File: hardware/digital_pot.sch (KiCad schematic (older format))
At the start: 98 parts

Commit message: dodano wyjscie programatora, przyciski ustalono wysjcie i2c, dodany plik CubeMX z pinouterm
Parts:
- added C? (x6): 100n, symbol Device:C
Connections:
- net +5V: now also C?.2, C?.2, C?.2, C?.2, C?.2, C?.2
- net GND: now also C?.1, C?.1, C?.1, C?.1, C?.1, C?.1
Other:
- moved on the sheet: C?, R?, U?A, U?B, U?D

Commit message: DRC przechodzi dorzucone złącze do wyświetlacza na i2c oraz jeden push button
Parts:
- gave numbers to parts that had none: 80

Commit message: przypisano footprinty
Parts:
- C12, C13, C14, C15, C16, C17, C18, C19, C20, C21, C22, C23, C24, C25, C26, C27, C28, C29, C30, C31, C32, C33, C34, C35, C36, C37, C38, C39, C40, C41, C42, C43, C44, C45, C46, C47, C48, C49, C50, C51, C52, C53, C54, C55, C56, C57, C58, C59: footprint (none) -> Capacitor_SMD:C_0603_1608Metric_Pad1.05x0.95mm_HandSolder
- R10, R11, R12, R13, R14, R15, R16, R17, R18, R19, R20, R21, R6, R7, R8, R9: footprint (none) -> Resistor_SMD:R_0603_1608Metric_Pad1.05x0.95mm_HandSolder
- U10, U13, U14, U15, U16, U17, U4, U7: footprint (none) -> Package_SO:SOIC-14_3.9x8.7mm_P1.27mm

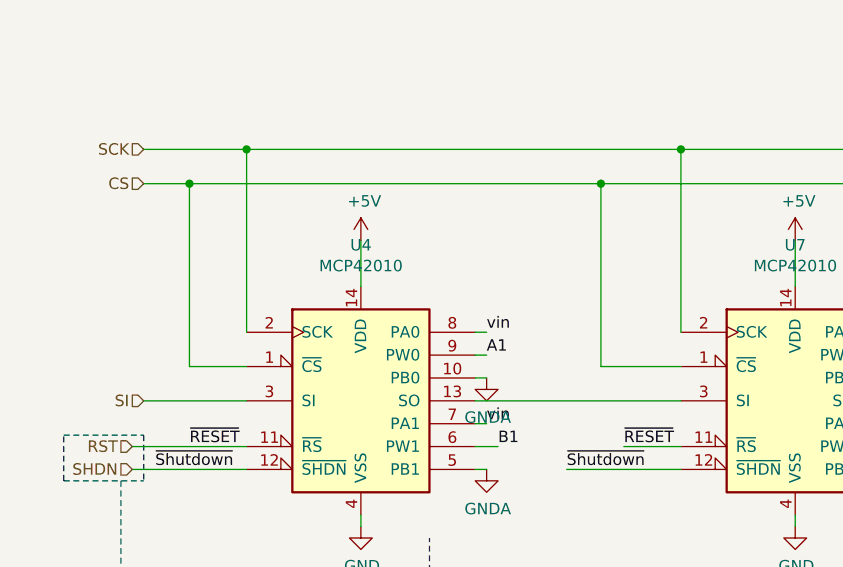
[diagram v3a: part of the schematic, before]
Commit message: Dodenie pullup do spi i i2c
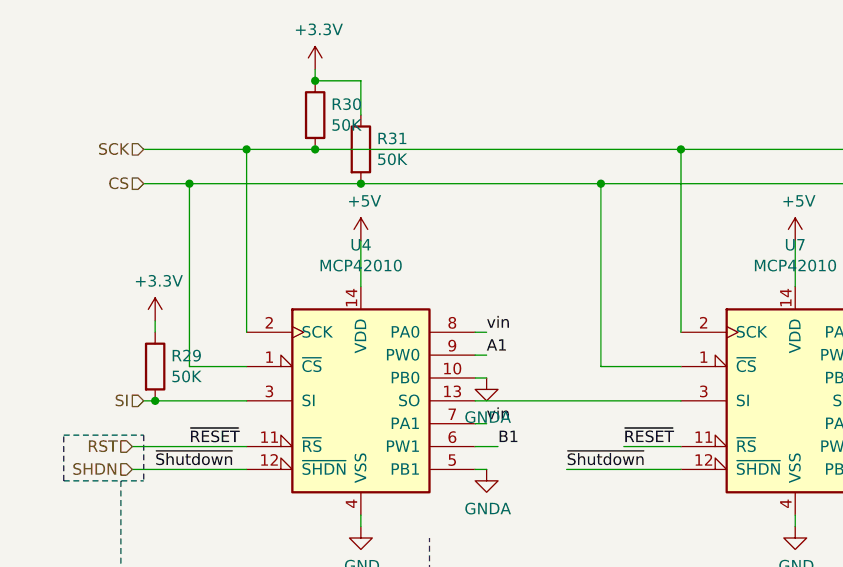
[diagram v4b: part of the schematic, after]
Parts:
- added R29, R30, R31: 50K, Resistor_SMD:R_0603_1608Metric_Pad1.05x0.95mm_HandSolder, symbol Device:R
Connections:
- net CS: now also R31.2
- net SCK: now also R30.2
- net SI: now also R29.2
- new net +3V3: R29.1, R30.1, R31.1
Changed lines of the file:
@@
 	1550 1750 1550 950
 Wire Wire Line
-	1550 950  1100 950
-Wire Wire Line
-	1550 950  3450 950
+	1550 950  1850 950
 Wire Wire Line
 	9300 950  9300 1750
@@
 	1300 1900 1550 1900
 Wire Wire Line
-	1300 1100 3100 1100
+	1300 1100 2050 1100
 Connection ~ 1300 1100
 Wire Wire Line
@@
 Connection ~ 3100 1100
 Wire Wire Line
-	1100 2050 1550 2050
+	1100 2050 1150 2050
 Text HLabel 1100 2050 0    50   Input ~ 0
 SI
@@
 Wire Wire Line
 	4700 7050 4400 7050
+$Comp
+L power:+3.3V #PWR0144
+U 1 1 5D367B76
+P 1850 600
+F 0 "#PWR0144" H 1850 450 50  0001 C CNN
+F 1 "+3.3V" H 1865 773 50  0000 C CNN
+F 2 "" H 1850 600 50  0001 C CNN
+F 3 "" H 1850 600 50  0001 C CNN
+	1    1850 600
+	1    0    0    -1
+$EndComp
+$Comp
+L Device:R R30
+U 1 1 5D36BDF5
+P 1850 800
+F 0 "R30" H 1920 846 50  0000 L CNN
+F 1 "50K" H 1920 755 50  0000 L CNN
+F 2 "Resistor_SMD:R_0603_1608Metric_Pad1.05x0.95mm_HandSolder" V 1780 800 50  0001 C CNN
+F 3 "~" H 1850 800 50  0001 C CNN
+	1    1850 800
+	1    0    0    -1
+$EndComp
+$Comp
+L Device:R R31
+U 1 1 5D36D3BE
+P 2050 950
+F 0 "R31" H 2120 996 50  0000 L CNN
+F 1 "50K" H 2120 905 50  0000 L CNN
+F 2 "Resistor_SMD:R_0603_1608Metric_Pad1.05x0.95mm_HandSolder" V 1980 950 50  0001 C CNN
+F 3 "~" H 2050 950 50  0001 C CNN
+	1    2050 950
+	1    0    0    -1
+$EndComp
+Connection ~ 2050 1100
+Wire Wire Line
+	2050 1100 3100 1100
+Connection ~ 1850 950
+Wire Wire Line
+	1850 950  3450 950
+Wire Wire Line
+	1850 600  1850 650
+Wire Wire Line
+	1100 950  1550 950
+Wire Wire Line
+	1850 650  2050 650
+Wire Wire Line
+	2050 650  2050 800
+Connection ~ 1850 650
+$Comp
+L Device:R R29
+U 1 1 5D41841E
+P 1150 1900
+F 0 "R29" H 1220 1946 50  0000 L CNN
+F 1 "50K" H 1220 1855 50  0000 L CNN
+F 2 "Resistor_SMD:R_0603_1608Metric_Pad1.05x0.95mm_HandSolder" V 1080 1900 50  0001 C CNN
+F 3 "~" H 1150 1900 50  0001 C CNN
+	1    1150 1900
+	1    0    0    -1
+$EndComp
+Connection ~ 1150 2050
+Wire Wire Line
+	1150 2050 1550 2050
+$Comp
+L power:+3.3V #PWR0143
+U 1 1 5D41881E
+P 1150 1700
+F 0 "#PWR0143" H 1150 1550 50  0001 C CNN
+F 1 "+3.3V" H 1165 1873 50  0000 C CNN
+F 2 "" H 1150 1700 50  0001 C CNN
+F 3 "" H 1150 1700 50  0001 C CNN
+	1    1150 1700
+	1    0    0    -1
+$EndComp
+Wire Wire Line
+	1150 1700 1150 1750
 $EndSCHEMATC

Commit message: pierwszy układ PCB
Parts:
- U11, U12, U2, U3, U5, U6, U8, U9: footprint Package_SO:SOIC-8-1EP_3.9x4.9mm_P1.27mm_EP2.41x3.81mm -> Package_SO:SOIC-14_3.9x8.7mm_P1.27mm

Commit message: dodanie zabezpieczen portów i dzialniki napiec na wejsciach adc
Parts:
- added R20, R24, R30, R32, R36, R40, R46, R48: 220k, Resistor_SMD:R_0603_1608Metric_Pad1.05x0.95mm_HandSolder, symbol Device:R
- added R21, R25, R31, R33, R37, R41, R47, R49: 330k, Resistor_SMD:R_0603_1608Metric_Pad1.05x0.95mm_HandSolder, symbol Device:R
- renumbered C12 to C14, C13 to C15, C14 to C16, C15 to C17, C16 to C18, C17 to C19, C18 to C20, C19 to C21, C20 to C22, C21 to C23, C22 to C24, C23 to C25, C24 to C26, C25 to C27, C26 to C28, C27 to C29, C28 to C30, C29 to C31, C30 to C32, C31 to C33, C32 to C34, C33 to C35, C34 to C36, C35 to C37, C36 to C38, C37 to C39, C38 to C40, C39 to C41, C40 to C42, C41 to C43, C42 to C44, C43 to C45, C44 to C46, C45 to C47, C46 to C48, C47 to C49, C48 to C50, C49 to C51, C50 to C52, C51 to C53, C52 to C54, C53 to C55, C54 to C56, C55 to C57, C56 to C58, C57 to C59, C58 to C60, C59 to C61, R29 to R15, R30 to R16, R6 to R17, R7 to R18, R31 to R19, R8 to R22, R9 to R23, R10 to R26, R11 to R27, R12 to R28, R13 to R29, R14 to R34, R15 to R35, R16 to R38, R17 to R39, R18 to R42, R19 to R43, R20 to R44, R21 to R45
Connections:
- net GND: now also R21.2, R25.2, R31.2, R33.2, R37.2, R41.2, R47.2, R49.2
- net OUT1: now also R20.2, R21.1; no longer U2.8, U2.9 (-)
- net OUT2: now also R24.2, R25.1; no longer U3.8, U3.9 (-)
- net OUT3: now also R30.2, R31.1; no longer U5.8, U5.9 (-)
- net OUT4: now also R32.2, R33.1; no longer U6.8, U6.9 (-)
- net OUT5: now also R36.2, R37.1; no longer U8.8, U8.9 (-)
- net OUT6: now also R40.2, R41.1; no longer U9.8, U9.9 (-)
- net OUT7: now also R46.2, R47.1; no longer U11.8, U11.9 (-)
- net OUT8: now also R48.2, R49.1; no longer U12.8, U12.9 (-)
- new net: R20.1, U2.8, U2.9 (-)
- new net: R30.1, U5.8, U5.9 (-)
- new net: R24.1, U3.8, U3.9 (-)
- new net: R36.1, U8.8, U8.9 (-)
- new net: R32.1, U6.8, U6.9 (-)
- new net: R40.1, U9.8, U9.9 (-)
- new net: R48.1, U12.8, U12.9 (-)
- new net: R46.1, U11.8, U11.9 (-)
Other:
- moved on the sheet: R17, R18, R26, R27, R34, R35, R38, R39, U2A, U2B, U2D, U5A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

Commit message: mała poprawka przy kondensatorach od opampow
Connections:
- net +5V: now also C17.2, C19.2, C22.1, C24.1, C32.2, C34.2, C37.1, C39.1, C47.2, C49.2, C51.1, C53.1, C55.2, C57.2, C59.1, C61.1
- net GNDA: no longer C17.2, C19.2, C22.1, C24.1, C32.2, C34.2, C37.1, C39.1, C47.2, C49.2, C51.1, C53.1, C55.2, C57.2, C59.1, C61.1

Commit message: trwa układanie, dodane złacze golpin
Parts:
- added J8: Conn_02x08_Odd_Even, Connector_PinHeader_2.54mm:PinHeader_2x08_P2.54mm_Vertical, symbol Connector_Generic:Conn_02x08_Odd_Even
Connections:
- net GNDA: now also J8.10 (Pin_10), J8.12 (Pin_12), J8.14 (Pin_14), J8.16 (Pin_16), J8.2 (Pin_2), J8.4 (Pin_4), J8.6 (Pin_6), J8.8 (Pin_8)
- net pot1: now reaches R20.1, U2.8, U2.9 (-)
- net pot1: now also J8.15 (Pin_15)
- net pot3: now reaches R30.1, U5.8, U5.9 (-)
- net pot3: now also J8.11 (Pin_11)
- net pot2: now reaches R24.1, U3.8, U3.9 (-)
- net pot2: now also J8.13 (Pin_13)
- net pot5: now reaches R36.1, U8.8, U8.9 (-)
- net pot5: now also J8.7 (Pin_7)
- net pot4: now reaches R32.1, U6.8, U6.9 (-)
- net pot4: now also J8.9 (Pin_9)
- net pot6: now reaches R40.1, U9.8, U9.9 (-)
- net pot6: now also J8.5 (Pin_5)
- net pot8: now reaches R48.1, U12.8, U12.9 (-)
- net pot8: now also J8.1 (Pin_1)
- net pot7: now reaches R46.1, U11.8, U11.9 (-)
- net pot7: now also J8.3 (Pin_3)
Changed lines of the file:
@@
 	15100 6250 15100 6300
 $Comp
-L power:+5V #PWR?
+L power:+5V #PWR0106
 U 1 1 5CE4F10B
 P 1300 9050
-F 0 "#PWR?" H 1300 8900 50  0001 C CNN
+F 0 "#PWR0106" H 1300 8900 50  0001 C CNN
 F 1 "+5V" H 1315 9223 50  0000 C CNN
 F 2 "" H 1300 9050 50  0001 C CNN
@@
 $EndComp
 $Comp
-L power:+5V #PWR?
+L power:+5V #PWR0108
 U 1 1 5CE4F569
 P 2000 9050
-F 0 "#PWR?" H 2000 8900 50  0001 C CNN
+F 0 "#PWR0108" H 2000 8900 50  0001 C CNN
 F 1 "+5V" H 2015 9223 50  0000 C CNN
 F 2 "" H 2000 9050 50  0001 C CNN
@@
 $EndComp
 $Comp
-L power:+5V #PWR?
+L power:+5V #PWR0166
 U 1 1 5CFD4ADA
 P 3050 9050
-F 0 "#PWR?" H 3050 8900 50  0001 C CNN
+F 0 "#PWR0166" H 3050 8900 50  0001 C CNN
 F 1 "+5V" H 3065 9223 50  0000 C CNN
 F 2 "" H 3050 9050 50  0001 C CNN
@@
 $EndComp
 $Comp
-L power:+5V #PWR?
+L power:+5V #PWR0167
 U 1 1 5CFD4AE0
 P 3750 9050
-F 0 "#PWR?" H 3750 8900 50  0001 C CNN
+F 0 "#PWR0167" H 3750 8900 50  0001 C CNN
 F 1 "+5V" H 3765 9223 50  0000 C CNN
 F 2 "" H 3750 9050 50  0001 C CNN
@@
 $EndComp
 $Comp
-L power:+5V #PWR?
+L power:+5V #PWR0168
 U 1 1 5D0058C1
 P 4900 9000
-F 0 "#PWR?" H 4900 8850 50  0001 C CNN
+F 0 "#PWR0168" H 4900 8850 50  0001 C CNN
 F 1 "+5V" H 4915 9173 50  0000 C CNN
 F 2 "" H 4900 9000 50  0001 C CNN
@@
 $EndComp
 $Comp
-L power:+5V #PWR?
+L power:+5V #PWR0169
 U 1 1 5D0058C7
 P 5600 9000
-F 0 "#PWR?" H 5600 8850 50  0001 C CNN
+F 0 "#PWR0169" H 5600 8850 50  0001 C CNN
 F 1 "+5V" H 5615 9173 50  0000 C CNN
 F 2 "" H 5600 9000 50  0001 C CNN
@@
 $EndComp
 $Comp
-L power:+5V #PWR?
+L power:+5V #PWR0170
 U 1 1 5D035F3C
 P 6750 8950
-F 0 "#PWR?" H 6750 8800 50  0001 C CNN
+F 0 "#PWR0170" H 6750 8800 50  0001 C CNN
 F 1 "+5V" H 6765 9123 50  0000 C CNN
 F 2 "" H 6750 8950 50  0001 C CNN
@@
 $EndComp
 $Comp
-L power:+5V #PWR?
+L power:+5V #PWR0171
 U 1 1 5D035F42
 P 7450 8950
-F 0 "#PWR?" H 7450 8800 50  0001 C CNN
+F 0 "#PWR0171" H 7450 8800 50  0001 C CNN
 F 1 "+5V" H 7465 9123 50  0000 C CNN
 F 2 "" H 7450 8950 50  0001 C CNN
@@
 $EndComp
 $Comp
-L power:+5V #PWR?
+L power:+5V #PWR0172
 U 1 1 5D066C3D
 P 6850 10500
-F 0 "#PWR?" H 6850 10350 50  0001 C CNN
+F 0 "#PWR0172" H 6850 10350 50  0001 C CNN
 F 1 "+5V" H 6865 10673 50  0000 C CNN
 F 2 "" H 6850 10500 50  0001 C CNN
@@
 $EndComp
 $Comp
-L power:+5V #PWR?
+L power:+5V #PWR0173
 U 1 1 5D066C43
 P 7550 10500
-F 0 "#PWR?" H 7550 10350 50  0001 C CNN
+F 0 "#PWR0173" H 7550 10350 50  0001 C CNN
 F 1 "+5V" H 7565 10673 50  0000 C CNN
 F 2 "" H 7550 10500 50  0001 C CNN
@@
 $EndComp
 $Comp
-L power:+5V #PWR?
+L power:+5V #PWR0174
 U 1 1 5D0976FA
 P 5000 10550
-F 0 "#PWR?" H 5000 10400 50  0001 C CNN
+F 0 "#PWR0174" H 5000 10400 50  0001 C CNN
 F 1 "+5V" H 5015 10723 50  0000 C CNN
 F 2 "" H 5000 10550 50  0001 C CNN
@@
 $EndComp
 $Comp
-L power:+5V #PWR?
+L power:+5V #PWR0175
 U 1 1 5D097700
 P 5700 10550
-F 0 "#PWR?" H 5700 10400 50  0001 C CNN
+F 0 "#PWR0175" H 5700 10400 50  0001 C CNN
 F 1 "+5V" H 5715 10723 50  0000 C CNN
 F 2 "" H 5700 10550 50  0001 C CNN
@@
 $EndComp
 $Comp
-L power:+5V #PWR?
+L power:+5V #PWR0176
 U 1 1 5D0C812B
 P 3000 10550
-F 0 "#PWR?" H 3000 10400 50  0001 C CNN
+F 0 "#PWR0176" H 3000 10400 50  0001 C CNN
 F 1 "+5V" H 3015 10723 50  0000 C CNN
 F 2 "" H 3000 10550 50  0001 C CNN
@@
 $EndComp
 $Comp
-L power:+5V #PWR?
+L power:+5V #PWR0177
 U 1 1 5D0C8131
 P 3700 10550
-F 0 "#PWR?" H 3700 10400 50  0001 C CNN
+F 0 "#PWR0177" H 3700 10400 50  0001 C CNN
 F 1 "+5V" H 3715 10723 50  0000 C CNN
 F 2 "" H 3700 10550 50  0001 C CNN
@@
 $EndComp
 $Comp
-L power:+5V #PWR?
+L power:+5V #PWR0178
 U 1 1 5D0F8BF2
 P 1250 10650
-F 0 "#PWR?" H 1250 10500 50  0001 C CNN
+F 0 "#PWR0178" H 1250 10500 50  0001 C CNN
 F 1 "+5V" H 1265 10823 50  0000 C CNN
 F 2 "" H 1250 10650 50  0001 C CNN
@@
 $EndComp
 $Comp
-L power:+5V #PWR?
+L power:+5V #PWR0179
 U 1 1 5D0F8BF8
 P 1950 10650
-F 0 "#PWR?" H 1950 10500 50  0001 C CNN
+F 0 "#PWR0179" H 1950 10500 50  0001 C CNN
 F 1 "+5V" H 1965 10823 50  0000 C CNN
 F 2 "" H 1950 10650 50  0001 C CNN
@@
 $EndComp
 $Comp
-L power:GNDA #PWR?
+L power:GNDA #PWR0180
 U 1 1 5D1290A9
 P 1250 9950
-F 0 "#PWR?" H 1250 9700 50  0001 C CNN
+F 0 "#PWR0180" H 1250 9700 50  0001 C CNN
 F 1 "GNDA" V 1255 9823 50  0000 R CNN
 F 2 "" H 1250 9950 50  0001 C CNN
@@
 $EndComp
 $Comp
-L power:GNDA #PWR?
+L power:GNDA #PWR0181
 U 1 1 5D129356
 P 1950 9950
-F 0 "#PWR?" H 1950 9700 50  0001 C CNN
+F 0 "#PWR0181" H 1950 9700 50  0001 C CNN
 F 1 "GNDA" V 1955 9822 50  0000 R CNN
 F 2 "" H 1950 9950 50  0001 C CNN
@@
 	0    -1   -1   0
 $EndComp
+Text Label 3150 4050 0    50   ~ 0
+pot1
+Text Label 5450 5550 0    50   ~ 0
+pot2
+Text Label 8400 7000 0    50   ~ 0
+pot3
+Text Label 9600 4350 0    50   ~ 0
+pot4
+Text Label 11450 6000 0    50   ~ 0
+pot5
+Text Label 12900 7650 0    50   ~ 0
+pot6
+Text Label 15100 5900 0    50   ~ 0
+pot7
+Text Label 15550 9100 0    50   ~ 0
+pot8
+Wire Wire Line
+	9500 9800 9850 9800
+Wire Wire Line
+	9500 9700 9850 9700
+Wire Wire Line
+	9850 9600 9500 9600
+Wire Wire Line
+	9500 9500 9850 9500
+Wire Wire Line
+	9850 9400 9500 9400
+Wire Wire Line
+	9500 9300 9850 9300
+Wire Wire Line
+	9850 9200 9500 9200
+Wire Wire Line
+	9500 9100 9850 9100
+Text Label 9500 9100 2    50   ~ 0
+pot8
+Text Label 9500 9200 2    50   ~ 0
+pot7
+Text Label 9500 9300 2    50   ~ 0
+pot6
+Text Label 9500 9400 2    50   ~ 0
+pot5
+Text Label 9500 9500 2    50   ~ 0
+pot4
+Text Label 9500 9600 2    50   ~ 0
+pot3
+Text Label 9500 9700 2    50   ~ 0
+pot2
+Text Label 9500 9800 2    50   ~ 0
+pot1
+$Comp
+L power:GNDA #PWR0182
+U 1 1 5D616EAB
+P 10350 9900
+F 0 "#PWR0182" H 10350 9650 50  0001 C CNN
+F 1 "GNDA" H 10355 9727 50  0000 C CNN
+F 2 "" H 10350 9900 50  0001 C CNN
+F 3 "" H 10350 9900 50  0001 C CNN
+	1    10350 9900
+	1    0    0    -1
+$EndComp
+$Comp
+L Connector_Generic:Conn_02x08_Odd_Even J8
+U 1 1 5D746B67
+P 10050 9400
+F 0 "J8" H 10100 9917 50  0000 C CNN
+F 1 "Conn_02x08_Odd_Even" H 10100 9826 50  0000 C CNN
+F 2 "Connector_PinHeader_2.54mm:PinHeader_2x08_P2.54mm_Vertical" H 10050 9400 50  0001 C CNN
+F 3 "~" H 10050 9400 50  0001 C CNN
+	1    10050 9400
+	1    0    0    -1
+$EndComp
+Wire Wire Line
+	10350 9800 10350 9900
+Wire Wire Line
+	10350 9100 10350 9200
+Connection ~ 10350 9800
+Connection ~ 10350 9200
+Wire Wire Line
+	10350 9200 10350 9300
+Connection ~ 10350 9300
+Wire Wire Line
+	10350 9300 10350 9400
+Connection ~ 10350 9400
+Wire Wire Line
+	10350 9400 10350 9500
+Connection ~ 10350 9500
+Wire Wire Line
+	10350 9500 10350 9600
+Connection ~ 10350 9600
+Wire Wire Line
+	10350 9600 10350 9700
+Connection ~ 10350 9700
+Wire Wire Line
+	10350 9700 10350 9800
 $EndSCHEMATC
